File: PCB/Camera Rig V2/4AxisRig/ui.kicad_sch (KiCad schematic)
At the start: 3 parts, among them J1 Conn_01x04_Socket, SW3 RotaryEncoder_Switch

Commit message: PCB V2 first draft
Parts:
- removed J1: Conn_01x04_Socket, Connector_JST:JST_SH_BM04B-SRSS-TB_1x04-1MP_P1.00mm_Vertical, symbol Connector:Conn_01x04_Socket
- removed SW3: RotaryEncoder_Switch, symbol Device:RotaryEncoder_Switch
- added J1: Conn_01x05_Socket, Connector_JST:JST_SH_BM04B-SRSS-TB_1x04-1MP_P1.00mm_Vertical, symbol Connector:Conn_01x05_Socket
- added R46: 10k, Resistor_SMD:R_0603_1608Metric_Pad0.98x0.95mm_HandSolder, symbol Device:R_US
- added SW3: PEC11L-4120F-S0020, PEC11L-4120F-S0020:PEC11L-4x20F-Sxxx_BRN, symbol PEC11L-4120F-S0020:PEC11L-4120F-S0020
- C28: footprint (none) -> Capacitor_SMD:C_0603_1608Metric_Pad1.08x0.95mm_HandSolder
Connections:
- net 3V3: now also J1.2 (Pin_2)
- net ENC_A: now also SW3.A
- net ENC_B: now also SW3.B
- net ENC_C: now also SW3.C
- net GND: now also J1.1 (Pin_1), SW3.SW1; no longer C28.2
- net I2C_SCL: now also J1.4 (Pin_4)
- net I2C_SDA: now also J1.3 (Pin_3)
- net SW: now also C28.2, R46.1
- new net: R46.2, SW3.SW2
- no-connect marks 0 -> 1
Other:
- moved on the sheet: C28

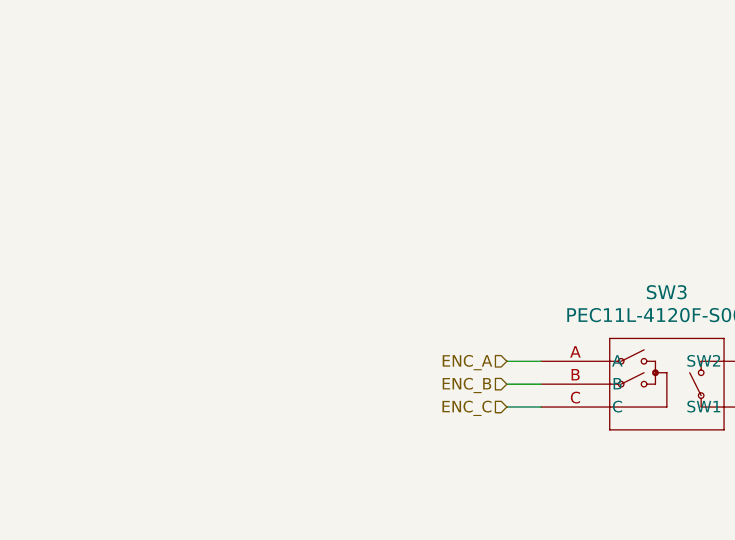
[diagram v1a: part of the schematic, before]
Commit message: Updated rotary encoder wiring
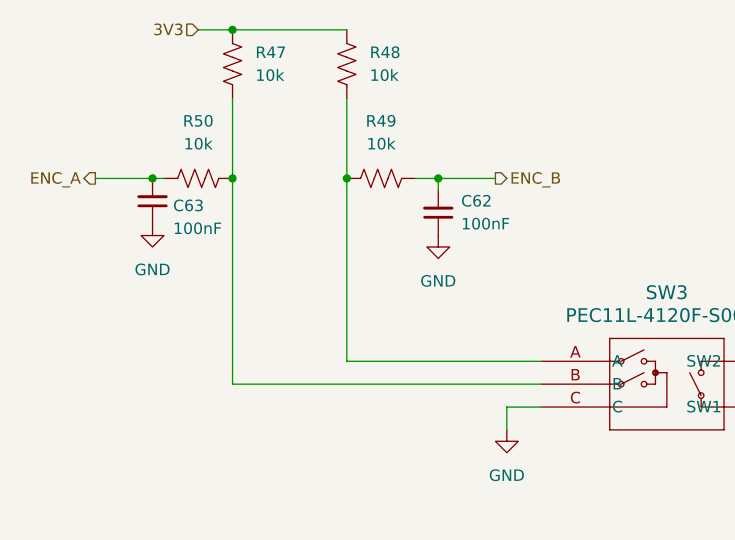
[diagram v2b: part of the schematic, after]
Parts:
- added C62, C63: 100nF, Capacitor_SMD:C_0603_1608Metric_Pad1.08x0.95mm_HandSolder, symbol Device:C_Small
- added R47, R48, R49, R50: 10k, Resistor_SMD:R_0603_1608Metric_Pad0.98x0.95mm_HandSolder, symbol Device:R_US
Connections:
- net ENC_C is gone; now on net GND: SW3.C
- net 3V3: now also R47.1, R48.1
- net ENC_A: now also C63.2, R50.1; no longer SW3.A
- net ENC_B: now also C62.2, R49.2; no longer SW3.B
- net GND: now also C62.1, C63.1
- new net: R48.2, R49.1, SW3.A
- new net: R47.2, R50.2, SW3.B

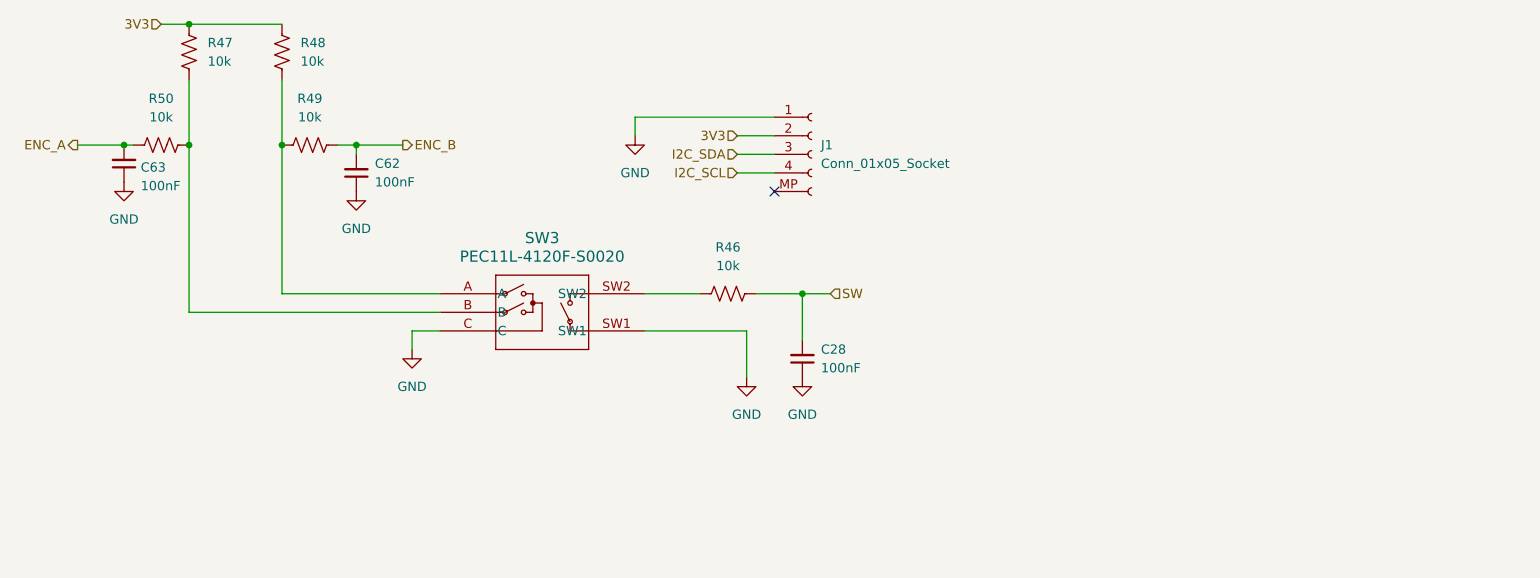
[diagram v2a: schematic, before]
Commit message: Netclass Improvements
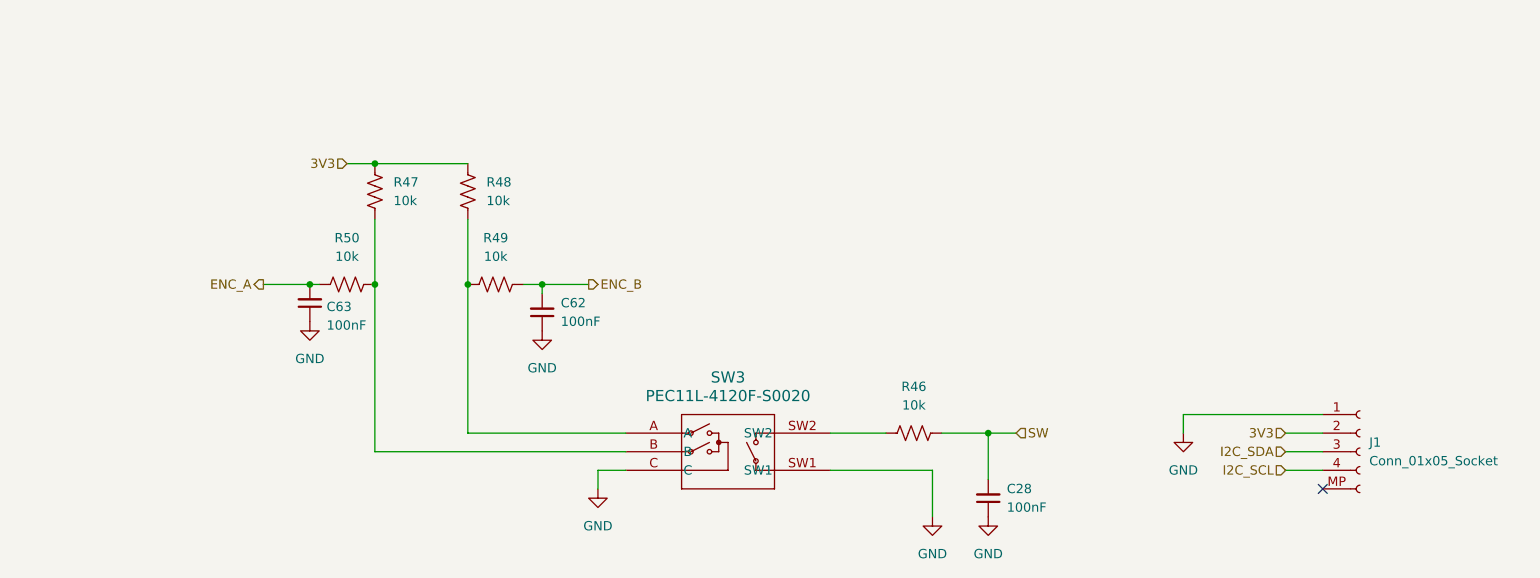
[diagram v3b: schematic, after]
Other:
- moved on the sheet: C28, C62, C63, J1, R46, R47, R48, R49, R50, SW3
